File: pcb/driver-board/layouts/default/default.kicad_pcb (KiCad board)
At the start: 2 copper layers, 6 parts

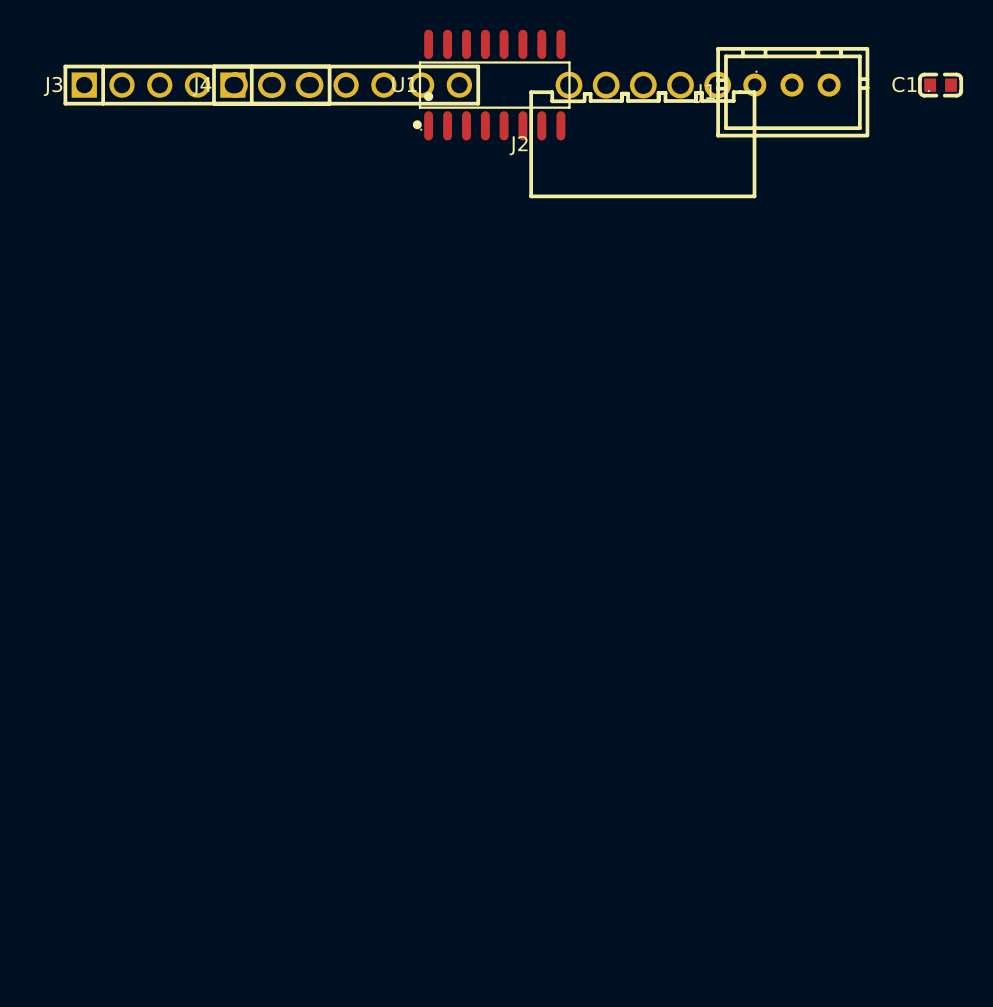
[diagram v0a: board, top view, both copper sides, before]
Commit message: feat(pcb): place driver board v1 + SVG preview renderer
place_and_render.py: address-keyed placement (survives rebuilds), edge
cuts, pads/silk/airwire SVG — no KiCad install needed. Parts lib patched:
'LCSC Part' property needed (at) or faebryk rotate_fp crashes.

Claude-Session: https://claude.ai/code/session_01SmZ7z8NecEFecH7qbexXiX
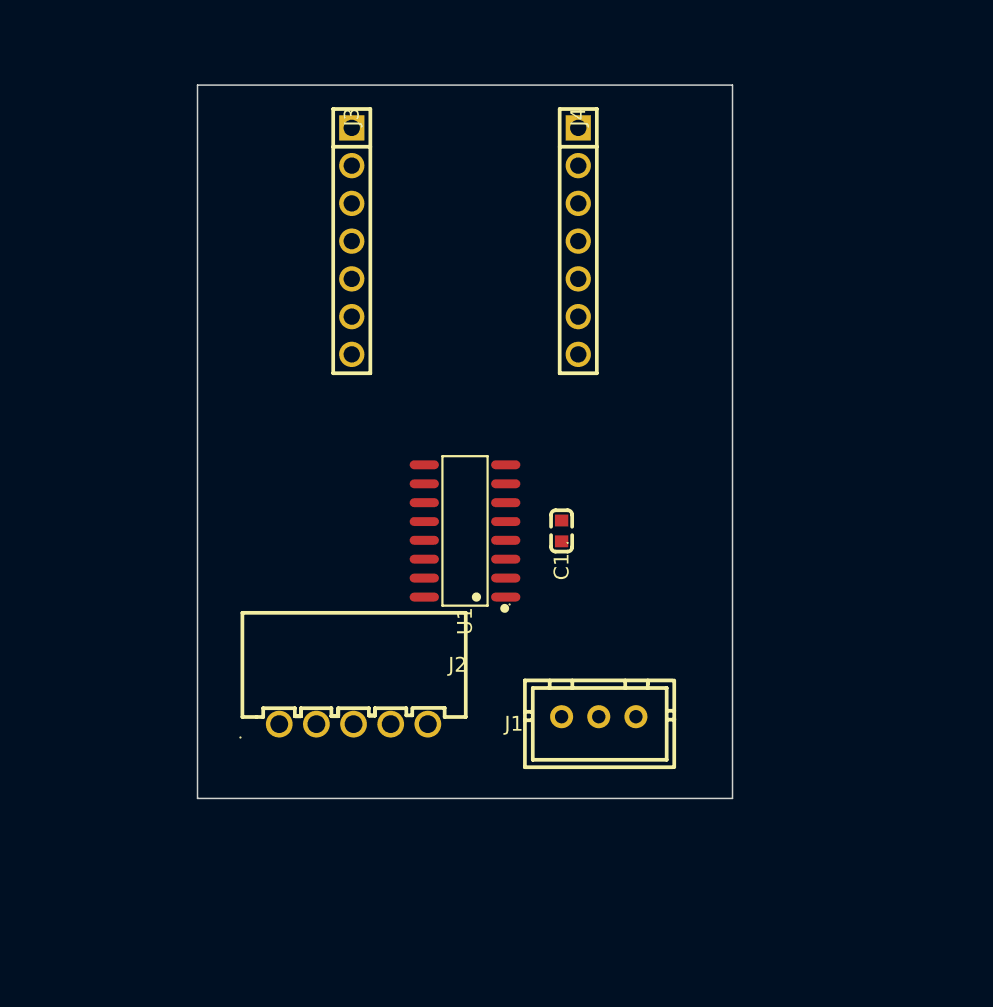
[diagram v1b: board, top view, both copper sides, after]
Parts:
- moved J2 47.2 mm to (10.5, 43.0), turned to 180 degrees
- moved J1 44.4 mm to (27.0, 42.5)
- moved C1 39.4 mm to (24.5, 30.0), turned to 90 degrees
- moved U1 30.1 mm to (18.0, 30.0), turned to 90 degrees
- moved J4 18.8 mm to (25.6, 10.5), turned to 270 degrees
- moved J3 14.8 mm to (10.4, 10.5), turned to 270 degrees
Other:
- board outline added: 36 x 48 mm

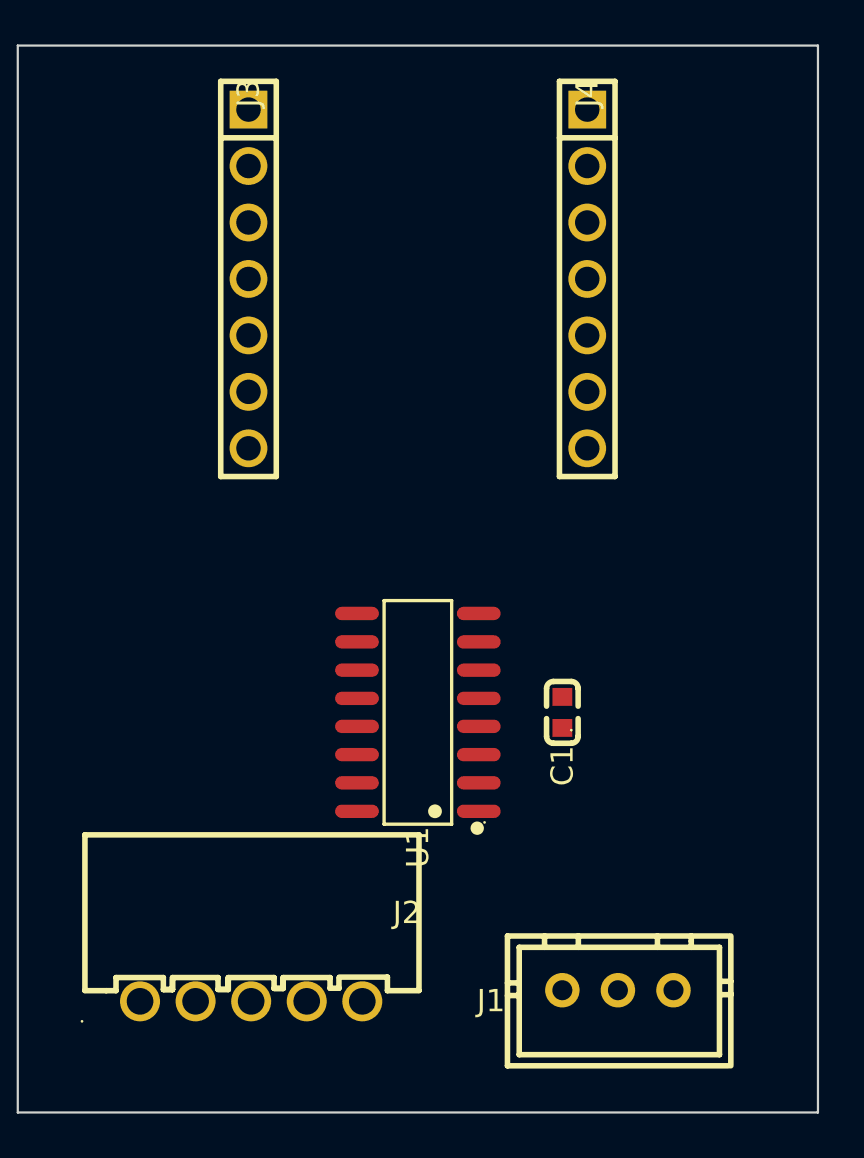
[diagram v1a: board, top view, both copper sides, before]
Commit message: feat(pcb): bulk cap + full hand-routing, 2-layer
220uF/16V electrolytic (C2887273) on 5V motor rail. Routes in
place_and_render.py: B.Cu spines/lanes, F.Cu stubs/fans; 0.8mm power,
0.4mm signal, 0.6/0.3 vias. All nets routed, no airwires left.

Claude-Session: https://claude.ai/code/session_01SmZ7z8NecEFecH7qbexXiX
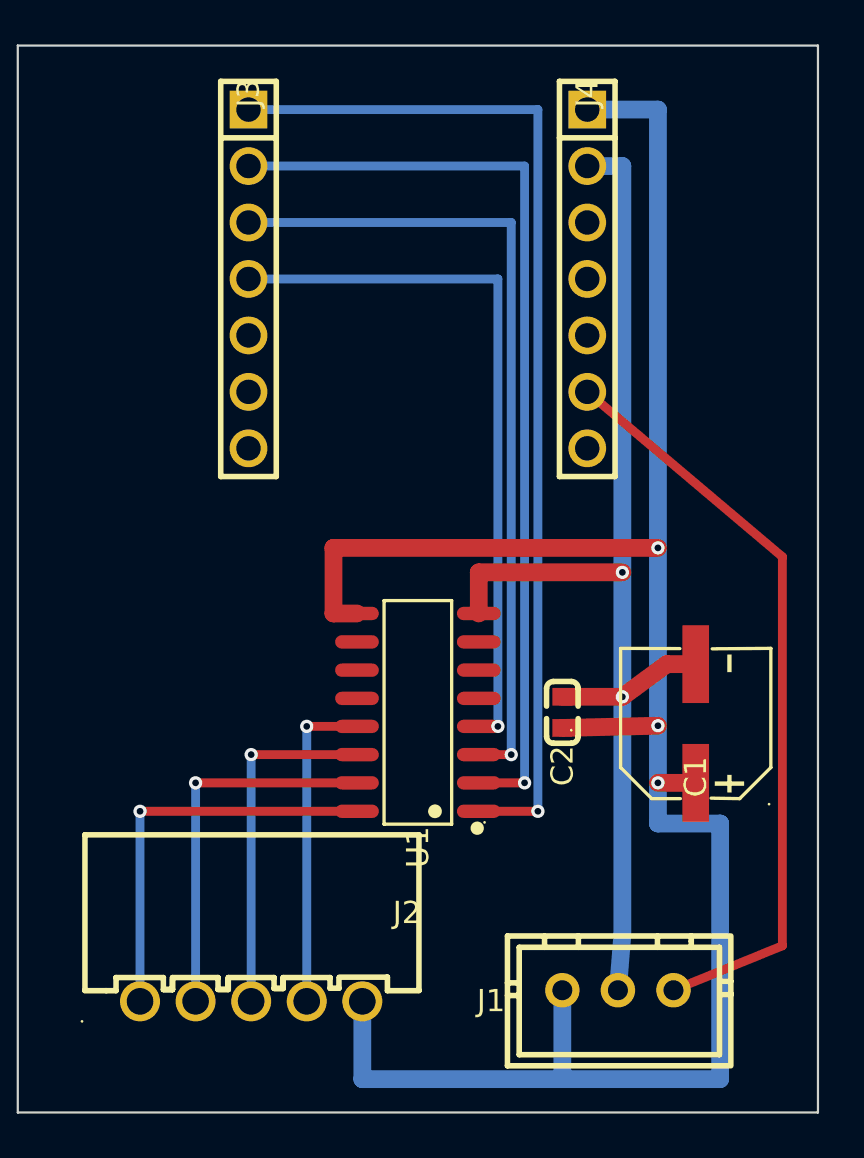
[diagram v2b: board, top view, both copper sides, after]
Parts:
- added C2: , CC0603_100NF:C0603, F.Cu at (24.5, 30.0)
- C1: footprint CC0603_100NF:C0603 -> CAP_220UF_16V:CAP-SMD_BD6.3-L6.6-W6.6-FD
- moved C1 6.02 mm to (30.5, 30.5)
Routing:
- net 1: track 0.00 -> 97.8 mm, vias 0 -> 3
- net 2: track 0.00 -> 53.5 mm, vias 0 -> 2
- net 1-1: track 0.00 -> 47.2 mm, vias 0 -> 1
- net 2-1: track 0.00 -> 42.2 mm, vias 0 -> 1
- net 3: track 0.00 -> 37.2 mm, vias 0 -> 1
- net hall_do: track 0.00 -> 34.3 mm
- net 4: track 0.00 -> 32.2 mm, vias 0 -> 1
- net 1-2: track 0.00 -> 18.3 mm, vias 0 -> 1
- net 15: track 0.00 -> 17.1 mm, vias 0 -> 1
- net 14: track 0.00 -> 15.9 mm, vias 0 -> 1
- net 13: track 0.00 -> 14.6 mm, vias 0 -> 1

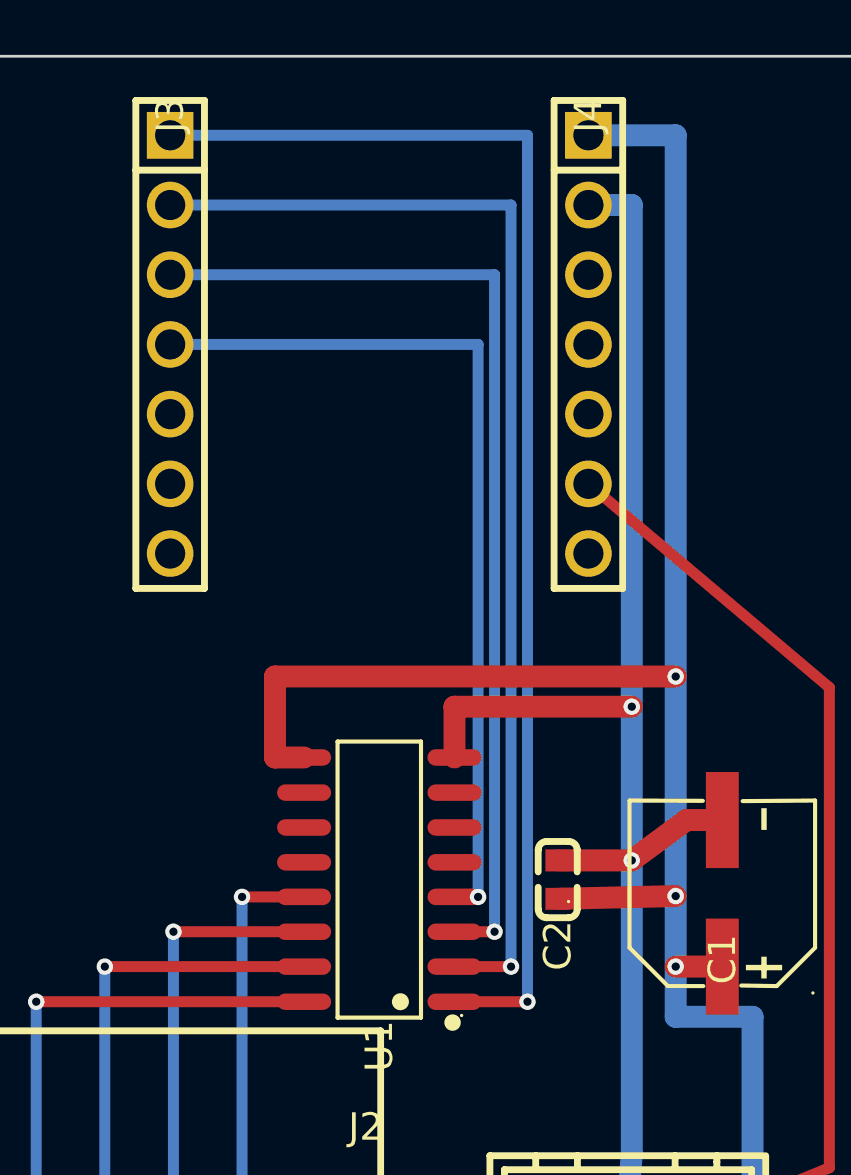
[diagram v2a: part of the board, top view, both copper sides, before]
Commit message: fix(pcb): lane pitch 0.75mm — KiCad DRC clean (0 err, 0 unconnected)
KiCad 10.0.4 installed (app copy from brew dmg; cask sudo step fails
headless). 3D renders via kicad-cli pcb render.

Claude-Session: https://claude.ai/code/session_01SmZ7z8NecEFecH7qbexXiX
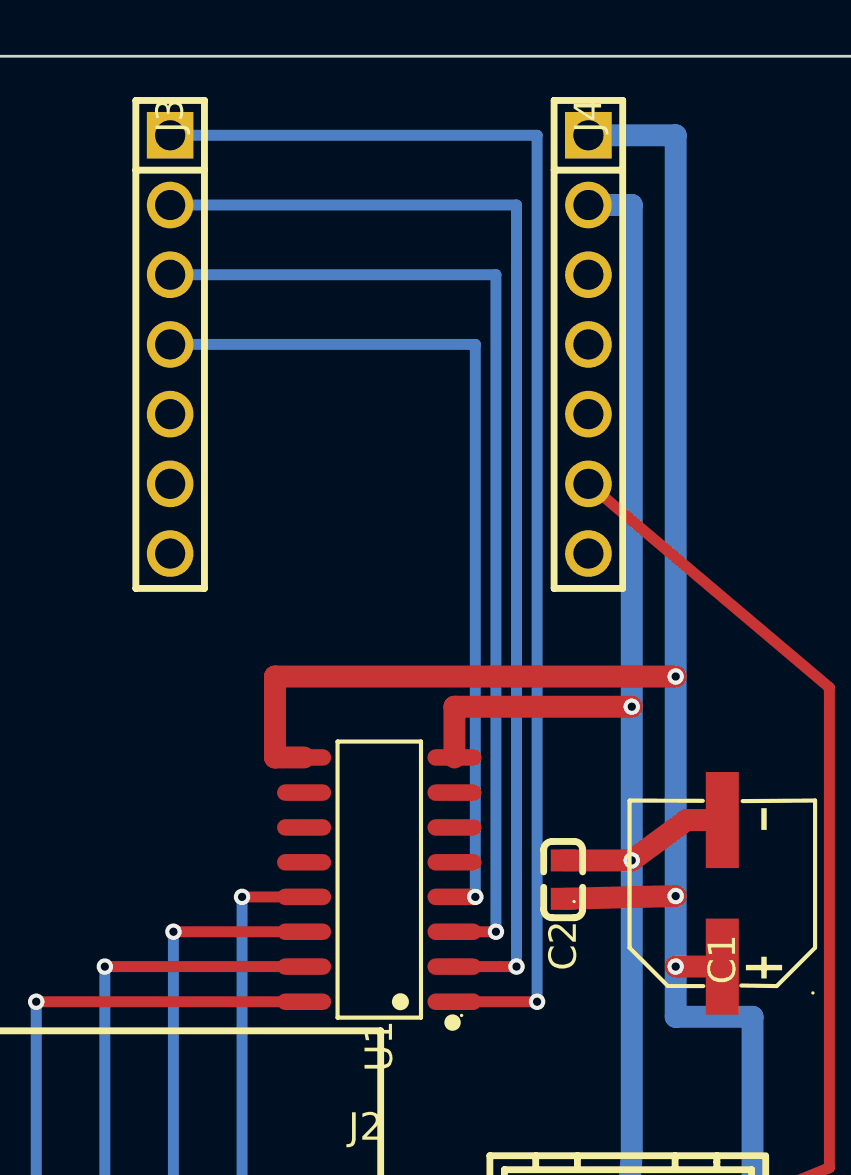
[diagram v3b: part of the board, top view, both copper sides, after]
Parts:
- moved C2 0.20 mm to (24.7, 30.0)
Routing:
- net 1-1: track 47.2 -> 48.0 mm
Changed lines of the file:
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@@
 	(footprint "CC0603_100NF:C0603"
 		(layer "F.Cu")
-		(at 24.5 30 90)
+		(at 24.7 30 90)
 		(descr "100nF (104) ±10% 50V")
 		(property "Reference" "C2"
@@
 	)
 	(via
-		(at 23.4 34.45)
+		(at 23.75 34.45)
 		(size 0.6)
 		(drill 0.3)
@@
 	)
 	(via
-		(at 22.8 33.17)
+		(at 23 33.17)
 		(size 0.6)
 		(drill 0.3)
@@
 	)
 	(via
-		(at 22.2 31.9)
+		(at 22.25 31.9)
 		(size 0.6)
 		(drill 0.3)
@@
 	)
 	(via
-		(at 21.6 30.63)
+		(at 21.5 30.63)
 		(size 0.6)
 		(drill 0.3)
@@
 	(segment
 		(start 10.38 2.88)
-		(end 23.4 2.88)
+		(end 23.75 2.88)
 		(width 0.4)
 		(layer "B.Cu")
@@
 	)
 	(segment
-		(start 23.4 2.88)
-		(end 23.4 34.45)
+		(start 23.75 2.88)
+		(end 23.75 34.45)
 		(width 0.4)
 		(layer "B.Cu")
@@
 	)
 	(segment
-		(start 23.4 34.45)
+		(start 23.75 34.45)
 		(end 20.74 34.45)
 		(width 0.4)
@@
 	(segment
 		(start 10.38 5.42)
-		(end 22.8 5.42)
+		(end 23 5.42)
 		(width 0.4)
 		(layer "B.Cu")
@@
 	)
 	(segment
-		(start 22.8 5.42)
-		(end 22.8 33.17)
+		(start 23 5.42)
+		(end 23 33.17)
 		(width 0.4)
 		(layer "B.Cu")
@@
 	)
 	(segment
-		(start 22.8 33.17)
+		(start 23 33.17)
 		(end 20.74 33.17)
 		(width 0.4)
@@
 	(segment
 		(start 10.38 7.96)
-		(end 22.2 7.96)
+		(end 22.25 7.96)
 		(width 0.4)
 		(layer "B.Cu")
@@
 	)
 	(segment
-		(start 22.2 7.96)
-		(end 22.2 31.9)
+		(start 22.25 7.96)
+		(end 22.25 31.9)
 		(width 0.4)
 		(layer "B.Cu")
@@
 	)
 	(segment
-		(start 22.2 31.9)
+		(start 22.25 31.9)
 		(end 20.74 31.9)
 		(width 0.4)
@@
 	(segment
 		(start 10.38 10.5)
-		(end 21.6 10.5)
+		(end 21.5 10.5)
 		(width 0.4)
 		(layer "B.Cu")
@@
 	)
 	(segment
-		(start 21.6 10.5)
-		(end 21.6 30.63)
+		(start 21.5 10.5)
+		(end 21.5 30.63)
 		(width 0.4)
 		(layer "B.Cu")
@@
 	)
 	(segment
-		(start 21.6 30.63)
+		(start 21.5 30.63)
 		(end 20.74 30.63)
 		(width 0.4)
@@
 	(segment
 		(start 28.8 30.6)
-		(end 24.5 30.7)
+		(end 24.7 30.7)
 		(width 0.8)
 		(layer "F.Cu")
@@
 	(segment
 		(start 27.2 29.3)
-		(end 24.5 29.3)
-		(width 0.8)
-		(layer "F.Cu")
+		(end 24.7 29.3)
+		(width 0.8)
+		(layer "F.Cu")

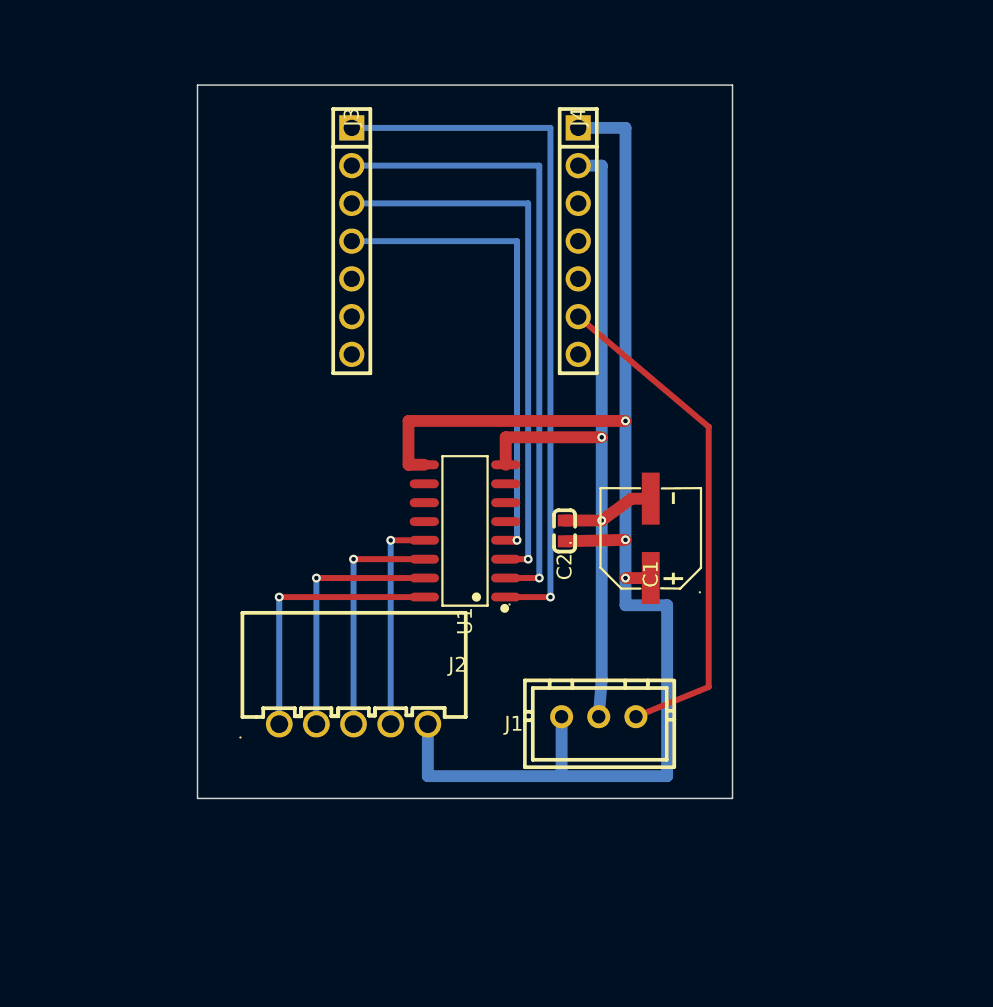
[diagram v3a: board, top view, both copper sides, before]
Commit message: feat(pcb): respin driver board to 45x60 with M3 mounts
The board had to fit behind a module; the plate is 95x118, so 36x48 was
never the constraint it looked like. Grow to 45x60 and use the slack:
every part now has comfortable hand-soldering clearance instead of the
0.35mm the XH-5 housing had to U1's lower pad row.

- board 36x48 -> 45x60, four M3 corner holes for heat-set inserts in the
  back shell
- j_motor rotated 180 -> 0 so the latch faces the board edge and the motor
  cable exits off-board rather than over the chip
- full re-route: B.Cu carries the four d-signal lanes and both power
  spines, F.Cu carries every power branch, so branches cross lanes on the
  far side
- board-level silk: title, pinout legend, connector labels
- move C1's refdes off its own pad and C2's clear of C1; drop the
  right-justify that skewed KiCad's text extent calculation

KiCad 10 installed, so this is the first time the board has seen real
DRC and a real 3D render rather than our own renderer's interpretation:
0 violations, 0 unconnected. Gerbers + drill exported to fab/.

Claude-Session: https://claude.ai/code/session_01UQXFTEy3DeBEx85CfiBq9q
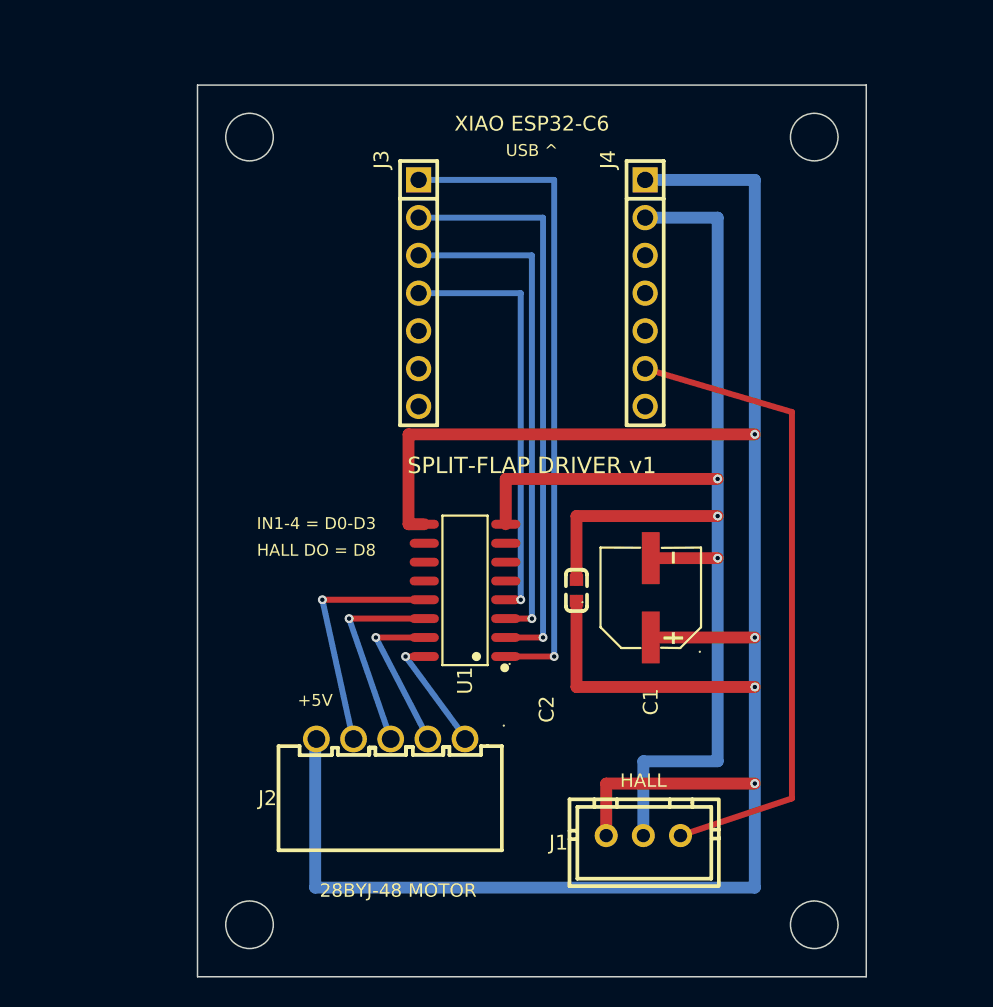
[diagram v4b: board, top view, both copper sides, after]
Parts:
- moved J1 8.54 mm to (30.0, 50.5)
- moved J3 5.70 mm to (14.9, 14.0)
- moved J4 5.70 mm to (30.1, 14.0)
- moved C2 4.08 mm to (25.5, 34.0)
- moved C1 4.00 mm to (30.5, 34.5)
- moved U1 4.00 mm to (18.0, 34.0)
- moved J2 2.69 mm to (13.0, 44.0), turned to 0 degrees
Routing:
- net 1: track 97.6 -> 163.3 mm, vias 3 -> 4
- net 2: track 53.3 -> 87.1 mm, vias 2 -> 3
- net 1-2: track 18.3 -> 8.15 mm
- net hall_do: track 34.3 -> 44.2 mm
- net 15: track 17.1 -> 11.0 mm
- net 4: track 32.0 -> 28.5 mm
- net 3: track 37.3 -> 33.8 mm
- net 2-1: track 42.6 -> 39.1 mm
- net 1-1: track 48.0 -> 44.5 mm
- net 14: track 15.9 -> 13.6 mm
- net 13: track 14.6 -> 16.5 mm
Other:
- board size 36 x 48 mm -> 45 x 60 mm
- board text added: "+5V"
- board text added: "28BYJ-48 MOTOR"
- board text added: "HALL"
- board text added: "HALL DO = D8"
- board text added: "IN1-4 = D0-D3"
- board text added: "SPLIT-FLAP DRIVER v1"
- board text added: "USB ^"
- board text added: "XIAO ESP32-C6"
